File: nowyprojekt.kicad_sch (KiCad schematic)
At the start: 42 parts, among them J1 Zasilanie, J2 01x03, J3 Conn_01x15_Pin, J4 Conn_01x15_Pin, Q1 BC856, Q2 BC856, Q3 BC856, Q4 BC856, U1 CA56-12SURKWA, U2 ATMEGA328P-AU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

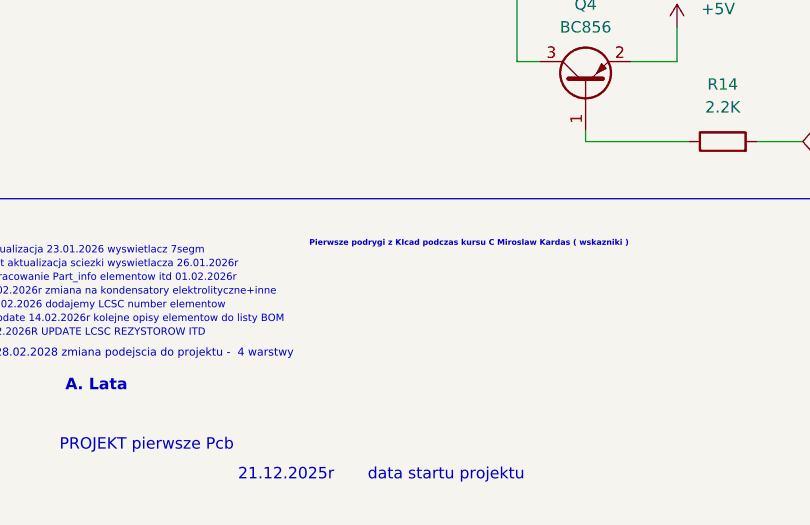
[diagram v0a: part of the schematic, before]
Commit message: dodanie do biblioteki kondensator 10nF
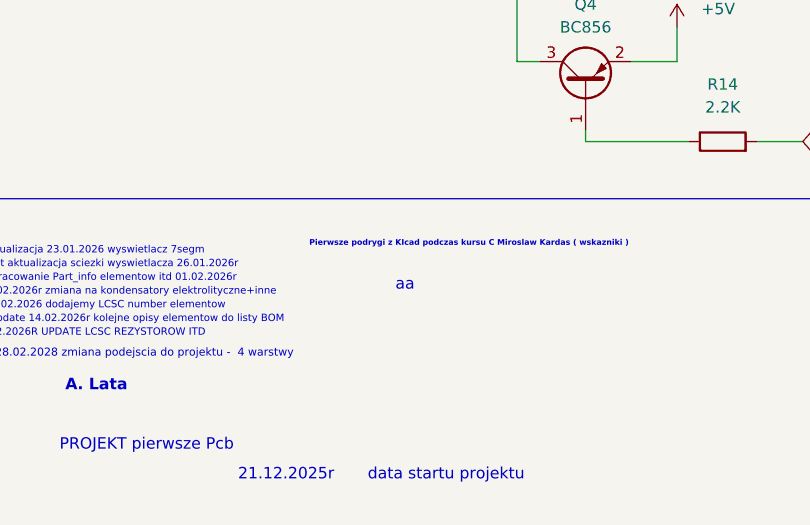
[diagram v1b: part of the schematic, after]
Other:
- note added: "aa"
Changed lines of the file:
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@@
+		)
+	)
+	(text "aa"
+		(exclude_from_sim no)
+		(at 226.314 172.212 0)
+		(effects
+			(font
+				(size 1.27 1.27)
+			)
 		)
 	)

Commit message: --
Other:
- note removed: "aa"
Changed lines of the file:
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@@
-		)
-	)
-	(text "aa"
-		(exclude_from_sim no)
-		(at 226.314 172.212 0)
-		(effects
-			(font
-				(size 1.27 1.27)
-			)
 		)
 	)

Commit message: maly update02.03.2026r
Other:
- note added: "01.03.2026 PRZEJSCIE NA GITHUB"
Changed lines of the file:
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@@
+		)
+	)
+	(text "01.03.2026 PRZEJSCIE NA GITHUB"
+		(exclude_from_sim no)
+		(at 195.58 180.848 0)
+		(effects
+			(font
+				(size 1.27 1.27)
+			)
 		)
 	)
@@
 	(text "28.02.2028 zmiana podejscia do projektu -  4 warstwy "
 		(exclude_from_sim no)
-		(at 197.358 179.832 0)
+		(at 196.85 179.07 0)
 		(effects
 			(font
